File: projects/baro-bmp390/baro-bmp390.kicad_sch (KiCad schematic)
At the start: 10 parts, among them J1 STEMMA-QT, U1 BMP390

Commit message: 9/6 update
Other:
- title: (none) -> BARO-BMP390 - Barometric Pressure Sensor Breakout
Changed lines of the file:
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@@
 	(generator_version "0.1")
 	(paper "A4")
+	(title_block
+		(title "BARO-BMP390 - Barometric Pressure Sensor Breakout")
+		(date "2026-08-24")
+		(rev "rev1")
+		(comment 1 "Lee Taeho")
+	)
 	(sheet_instances
 		(path "/"
@@
 		(instances
 			(project "baro-bmp390"
-				(path "/27a992b8-95f6-4d70-90dc-562ce1e640a5"
+				(path "/bfd5ee5d-0084-4396-b5d1-c0b6ab760dec"
 					(reference "J1")
 					(unit 1)
@@
 		(instances
 			(project "baro-bmp390"
-				(path "/27a992b8-95f6-4d70-90dc-562ce1e640a5"
+				(path "/bfd5ee5d-0084-4396-b5d1-c0b6ab760dec"
 					(reference "#PWR101")
 					(unit 1)
@@
 		(instances
 			(project "baro-bmp390"
-				(path "/27a992b8-95f6-4d70-90dc-562ce1e640a5"
+				(path "/bfd5ee5d-0084-4396-b5d1-c0b6ab760dec"
 					(reference "#PWR102")
 					(unit 1)
@@
 		(instances
 			(project "baro-bmp390"
-				(path "/27a992b8-95f6-4d70-90dc-562ce1e640a5"
+				(path "/bfd5ee5d-0084-4396-b5d1-c0b6ab760dec"
 					(reference "#FLG01")
 					(unit 1)
@@
 		(instances
 			(project "baro-bmp390"
-				(path "/27a992b8-95f6-4d70-90dc-562ce1e640a5"
+				(path "/bfd5ee5d-0084-4396-b5d1-c0b6ab760dec"
 					(reference "#PWR103")
 					(unit 1)
@@
 		(instances
 			(project "baro-bmp390"
-				(path "/27a992b8-95f6-4d70-90dc-562ce1e640a5"
+				(path "/bfd5ee5d-0084-4396-b5d1-c0b6ab760dec"
 					(reference "#FLG02")
 					(unit 1)
@@
 		(instances
 			(project "baro-bmp390"
-				(path "/27a992b8-95f6-4d70-90dc-562ce1e640a5"
+				(path "/bfd5ee5d-0084-4396-b5d1-c0b6ab760dec"
 					(reference "#PWR104")
 					(unit 1)
@@
 		(instances
 			(project "baro-bmp390"
-				(path "/27a992b8-95f6-4d70-90dc-562ce1e640a5"
+				(path "/bfd5ee5d-0084-4396-b5d1-c0b6ab760dec"
 					(reference "U1")
 					(unit 1)
@@
 		(instances
 			(project "baro-bmp390"
-				(path "/27a992b8-95f6-4d70-90dc-562ce1e640a5"
+				(path "/bfd5ee5d-0084-4396-b5d1-c0b6ab760dec"
 					(reference "C1")
 					(unit 1)
@@
 		(instances
 			(project "baro-bmp390"
-				(path "/27a992b8-95f6-4d70-90dc-562ce1e640a5"
+				(path "/bfd5ee5d-0084-4396-b5d1-c0b6ab760dec"
 					(reference "#PWR105")
 					(unit 1)
@@
 		(instances
 			(project "baro-bmp390"
-				(path "/27a992b8-95f6-4d70-90dc-562ce1e640a5"
+				(path "/bfd5ee5d-0084-4396-b5d1-c0b6ab760dec"
 					(reference "#PWR106")
 					(unit 1)
@@
 		(instances
 			(project "baro-bmp390"
-				(path "/27a992b8-95f6-4d70-90dc-562ce1e640a5"
+				(path "/bfd5ee5d-0084-4396-b5d1-c0b6ab760dec"
 					(reference "C2")
 					(unit 1)
@@
 		(instances
 			(project "baro-bmp390"
-				(path "/27a992b8-95f6-4d70-90dc-562ce1e640a5"
+				(path "/bfd5ee5d-0084-4396-b5d1-c0b6ab760dec"
 					(reference "#PWR107")
 					(unit 1)
@@
 		(instances
 			(project "baro-bmp390"
-				(path "/27a992b8-95f6-4d70-90dc-562ce1e640a5"
+				(path "/bfd5ee5d-0084-4396-b5d1-c0b6ab760dec"
 					(reference "#PWR108")
 					(unit 1)
@@
 		(instances
 			(project "baro-bmp390"
-				(path "/27a992b8-95f6-4d70-90dc-562ce1e640a5"
+				(path "/bfd5ee5d-0084-4396-b5d1-c0b6ab760dec"
 					(reference "C3")
 					(unit 1)
@@
 		(instances
 			(project "baro-bmp390"
-				(path "/27a992b8-95f6-4d70-90dc-562ce1e640a5"
+				(path "/bfd5ee5d-0084-4396-b5d1-c0b6ab760dec"
 					(reference "#PWR109")
 					(unit 1)
@@
 		(instances
 			(project "baro-bmp390"
-				(path "/27a992b8-95f6-4d70-90dc-562ce1e640a5"
+				(path "/bfd5ee5d-0084-4396-b5d1-c0b6ab760dec"
 					(reference "#PWR110")
 					(unit 1)
@@
 		(instances
 			(project "baro-bmp390"
-				(path "/27a992b8-95f6-4d70-90dc-562ce1e640a5"
+				(path "/bfd5ee5d-0084-4396-b5d1-c0b6ab760dec"
 					(reference "R1")
 					(unit 1)
@@
 		(instances
 			(project "baro-bmp390"
-				(path "/27a992b8-95f6-4d70-90dc-562ce1e640a5"
+				(path "/bfd5ee5d-0084-4396-b5d1-c0b6ab760dec"
 					(reference "#PWR111")
 					(unit 1)
@@
 		(instances
 			(project "baro-bmp390"
-				(path "/27a992b8-95f6-4d70-90dc-562ce1e640a5"
+				(path "/bfd5ee5d-0084-4396-b5d1-c0b6ab760dec"
 					(reference "R2")
 					(unit 1)
@@
 		(instances
 			(project "baro-bmp390"
-				(path "/27a992b8-95f6-4d70-90dc-562ce1e640a5"
+				(path "/bfd5ee5d-0084-4396-b5d1-c0b6ab760dec"
 					(reference "#PWR112")
 					(unit 1)
@@
 		(instances
 			(project "baro-bmp390"
-				(path "/27a992b8-95f6-4d70-90dc-562ce1e640a5"
+				(path "/bfd5ee5d-0084-4396-b5d1-c0b6ab760dec"
 					(reference "TP1")
 					(unit 1)
@@
 		(instances
 			(project "baro-bmp390"
-				(path "/27a992b8-95f6-4d70-90dc-562ce1e640a5"
+				(path "/bfd5ee5d-0084-4396-b5d1-c0b6ab760dec"
 					(reference "#PWR113")
 					(unit 1)
@@
 		(instances
 			(project "baro-bmp390"
-				(path "/27a992b8-95f6-4d70-90dc-562ce1e640a5"
+				(path "/bfd5ee5d-0084-4396-b5d1-c0b6ab760dec"
 					(reference "#PWR114")
 					(unit 1)
@@
 		(instances
 			(project "baro-bmp390"
-				(path "/27a992b8-95f6-4d70-90dc-562ce1e640a5"
+				(path "/bfd5ee5d-0084-4396-b5d1-c0b6ab760dec"
 					(reference "#PWR115")
 					(unit 1)
@@
 		(instances
 			(project "baro-bmp390"
-				(path "/27a992b8-95f6-4d70-90dc-562ce1e640a5"
+				(path "/bfd5ee5d-0084-4396-b5d1-c0b6ab760dec"
 					(reference "#PWR116")
 					(unit 1)
@@
 		(instances
 			(project "baro-bmp390"
-				(path "/27a992b8-95f6-4d70-90dc-562ce1e640a5"
+				(path "/bfd5ee5d-0084-4396-b5d1-c0b6ab760dec"
 					(reference "#PWR117")
 					(unit 1)
@@
 		(instances
 			(project "baro-bmp390"
-				(path "/27a992b8-95f6-4d70-90dc-562ce1e640a5"
+				(path "/bfd5ee5d-0084-4396-b5d1-c0b6ab760dec"
 					(reference "#PWR118")
 					(unit 1)
@@
 		(instances
 			(project "baro-bmp390"
-				(path "/27a992b8-95f6-4d70-90dc-562ce1e640a5"
+				(path "/bfd5ee5d-0084-4396-b5d1-c0b6ab760dec"
 					(reference "#PWR119")
 					(unit 1)
@@
 		(instances
 			(project "baro-bmp390"
-				(path "/27a992b8-95f6-4d70-90dc-562ce1e640a5"
+				(path "/bfd5ee5d-0084-4396-b5d1-c0b6ab760dec"
 					(reference "H1")
 					(unit 1)
@@
 		(instances
 			(project "baro-bmp390"
-				(path "/27a992b8-95f6-4d70-90dc-562ce1e640a5"
+				(path "/bfd5ee5d-0084-4396-b5d1-c0b6ab760dec"
 					(reference "H2")
 					(unit 1)

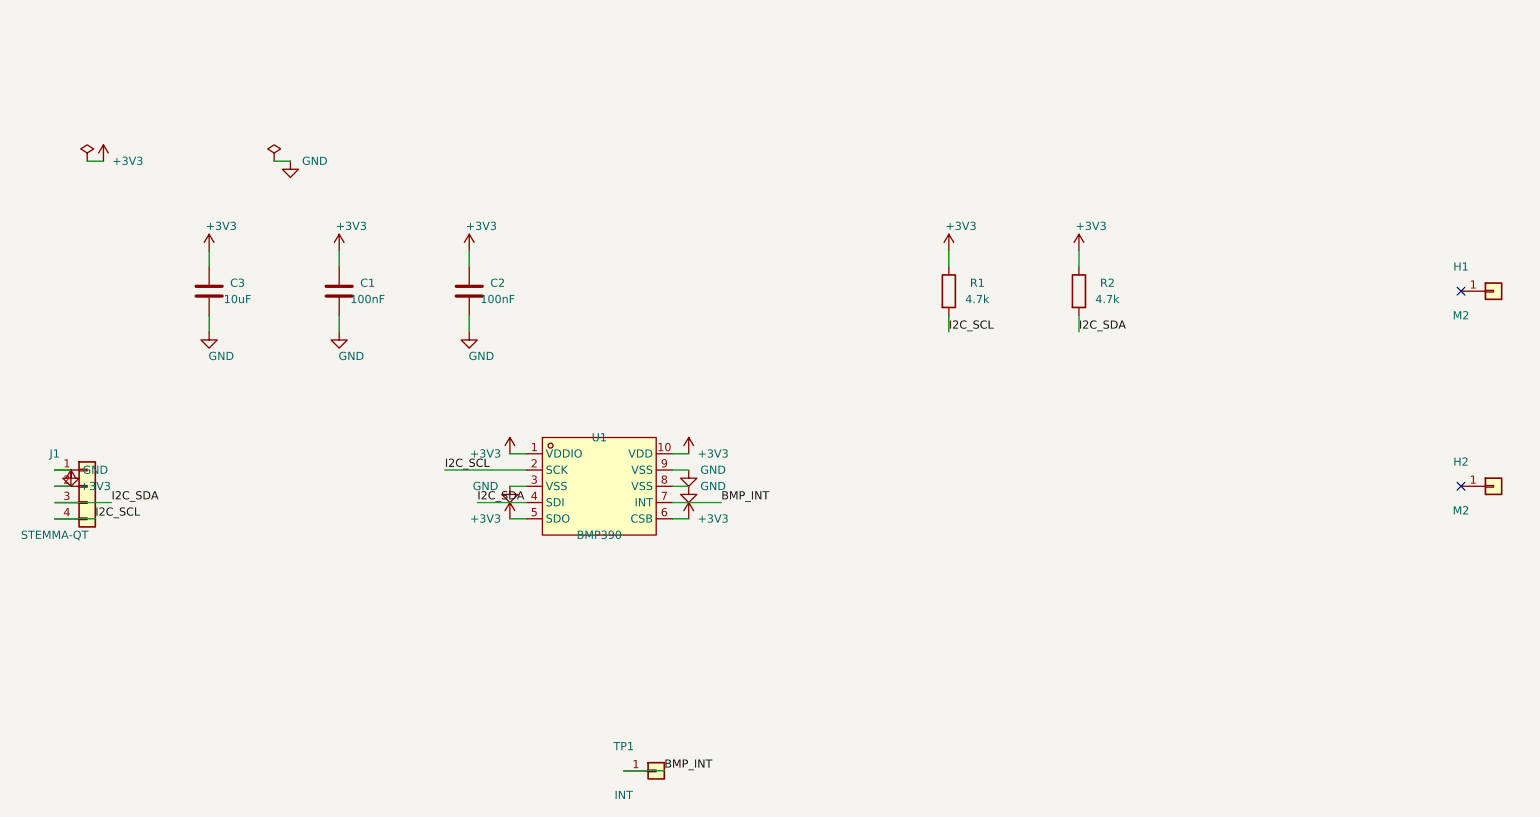
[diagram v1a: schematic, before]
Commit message: feat: promote BMP working schematic with parity gate
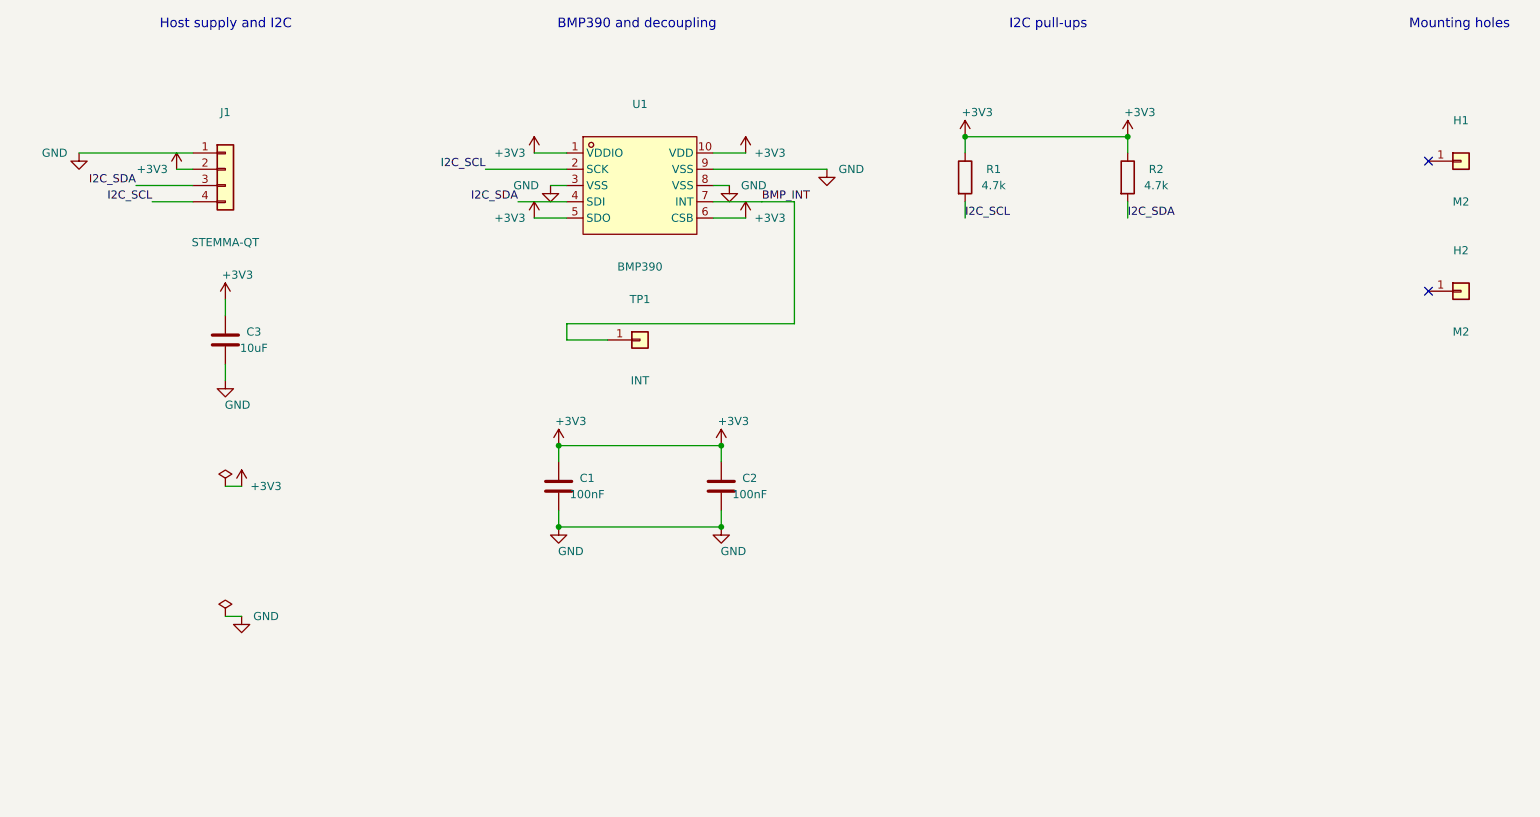
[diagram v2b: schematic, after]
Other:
- note added: "BMP390 and decoupling"
- note added: "Host supply and I2C"
- note added: "I2C pull-ups"
- note added: "Mounting holes"
- title: BARO-BMP390 - Barometric Pressure Sensor Breakout -> BMP390 - 3.3V I2C barometer
